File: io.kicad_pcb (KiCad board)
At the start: 2 copper layers, 107 x 58 mm, 98 parts, among them P1 CONN_01X04, P2 CONN_01X04, P3 CONN_01X04, P4 CONN_02X06, P5 CONN_02X09, Q1 VND7NV04, Q2 VND7NV04, Q3 VND7NV04, Q4 VND7NV04, Q5 VND7NV04, Q6 VND7NV04, U1 TC4427, U2 TC4427, U3 TC4427, U4 MCP2562-H/P, U5 LM2940

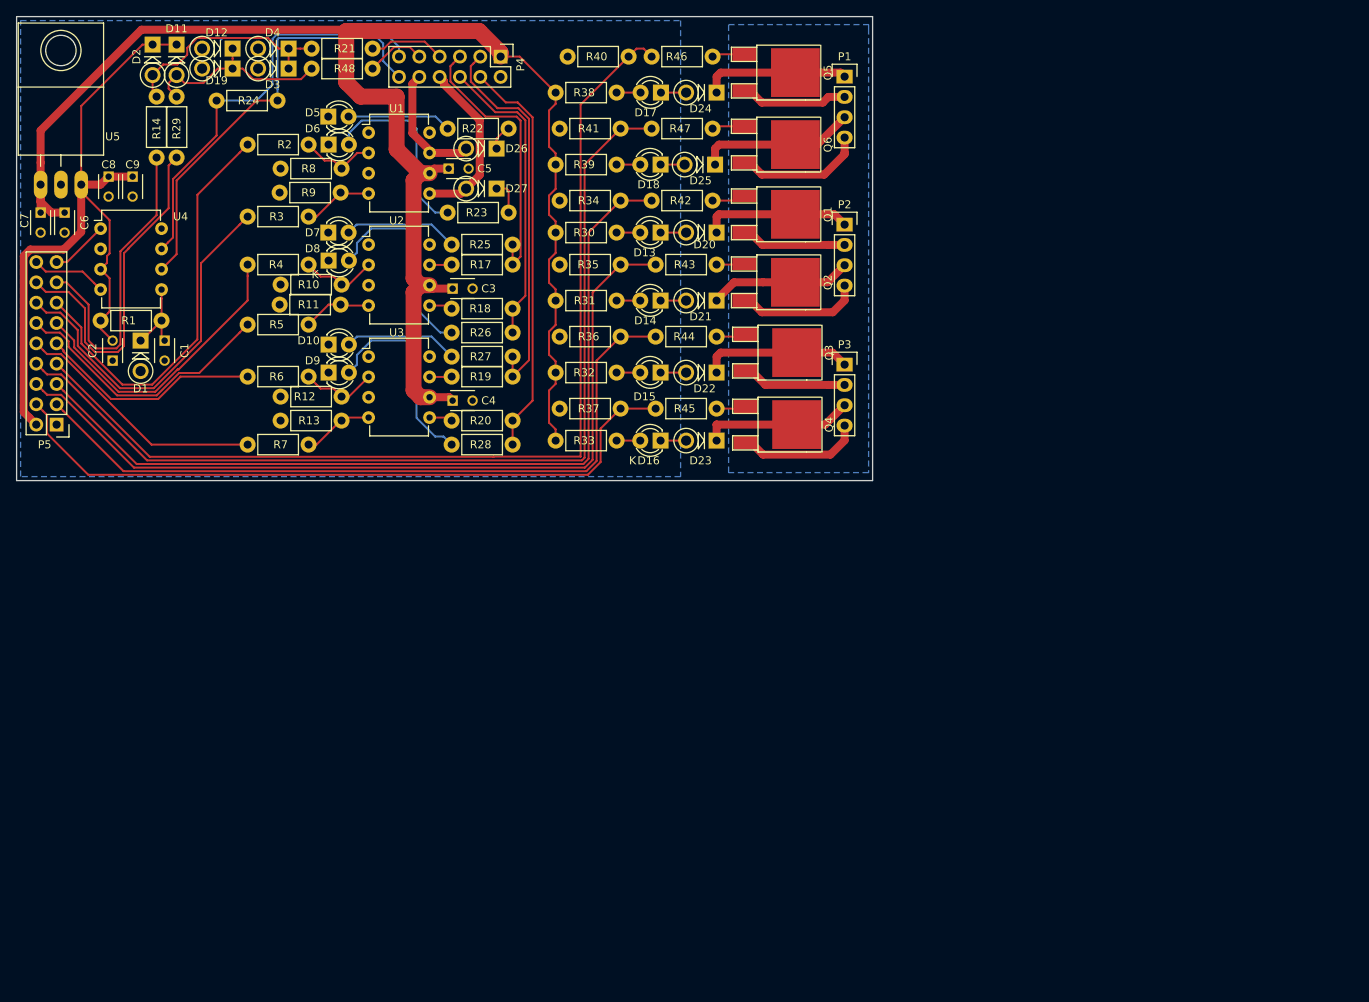
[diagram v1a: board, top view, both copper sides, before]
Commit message: Various updates to io board: - Add trigger inputs - Switch to 3v logic fets - switch to SMT components
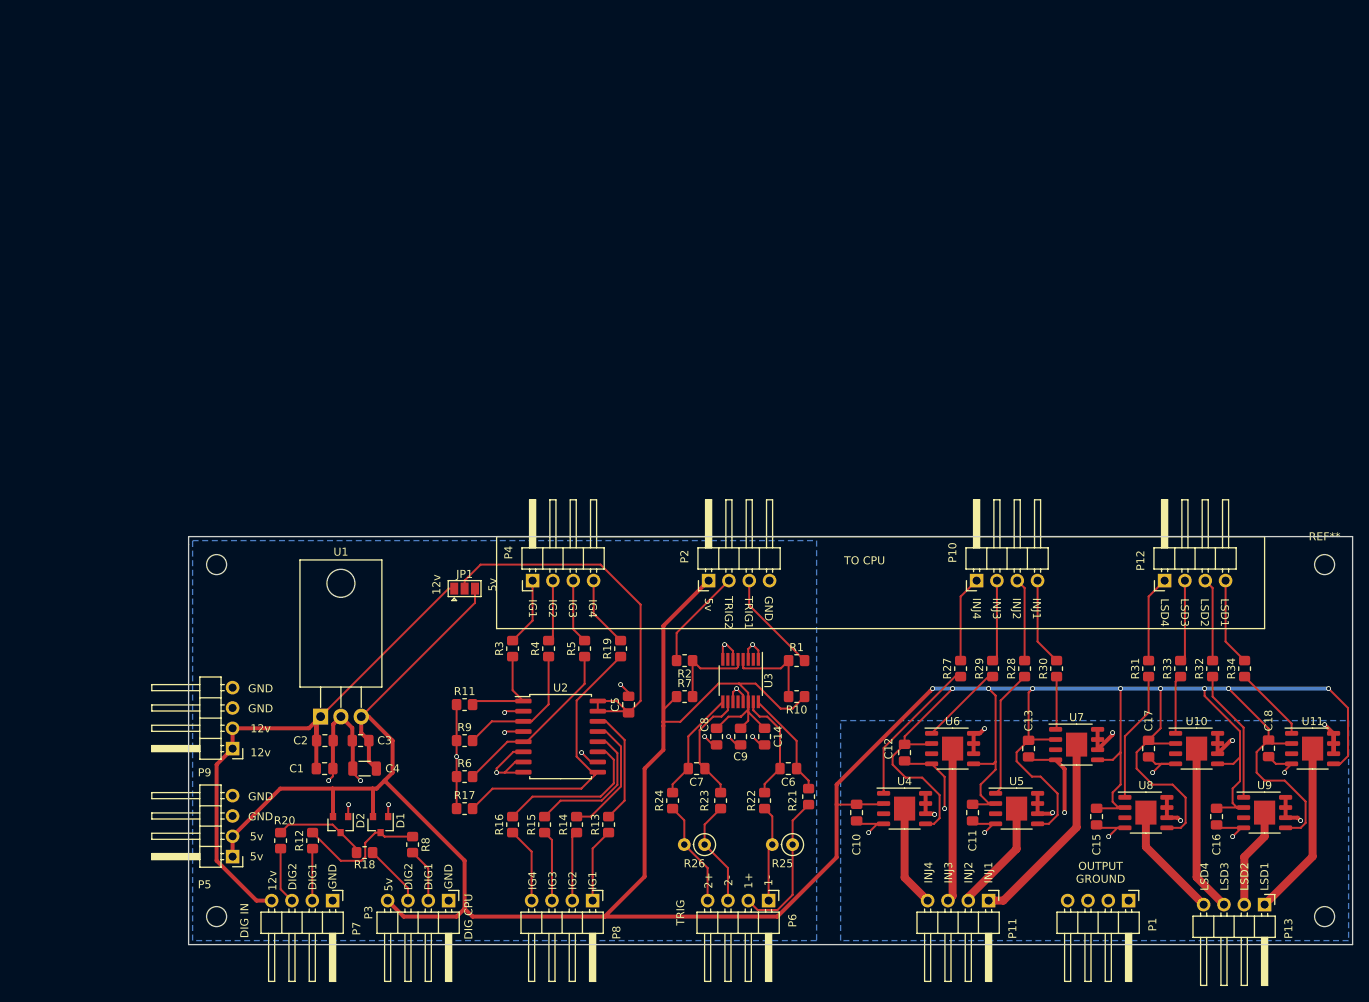
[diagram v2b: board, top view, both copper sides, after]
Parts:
- removed D10, D13, D14, D15, D16, D17, D18, D5, D6, D7, D8, D9: LED, LEDs:LED-3MM
- removed D11, D12, D20, D21, D22, D23, D24, D25, D26, D27, D3: D, Diodes_ThroughHole:Diode_DO-41_SOD81_Vertical_KathodeUp
- removed D19, D4: D_Zener, Diodes_ThroughHole:Diode_DO-41_SOD81_Vertical_KathodeUp
- removed Q1, Q2, Q3, Q4, Q5, Q6: VND7NV04, TO_SOT_Packages_SMD:TO-252-2Lead
- removed R35, R36, R37, R40, R41: 100k, Resistors_ThroughHole:Resistor_Horizontal_RM7mm
- removed R38, R39: 2.43k, Resistors_ThroughHole:Resistor_Horizontal_RM7mm
- removed R42, R43, R44, R45, R46, R47: 330, Resistors_ThroughHole:Resistor_Horizontal_RM7mm
- removed R48: 1k, Resistors_ThroughHole:Resistor_Horizontal_RM7mm
- added C10: .1uF, Capacitor_SMD:C_0805_2012Metric_Pad1.18x1.45mm_HandSolder, F.Cu at (118.5, 140.0)
- added C11: .1uF, Capacitor_SMD:C_0805_2012Metric_Pad1.18x1.45mm_HandSolder, F.Cu at (133.0, 140.0)
- added C12: .1uF, Capacitor_SMD:C_0805_2012Metric_Pad1.18x1.45mm_HandSolder, F.Cu at (124.5, 132.5)
- added C13: .1uF, Capacitor_SMD:C_0805_2012Metric_Pad1.18x1.45mm_HandSolder, F.Cu at (140.0, 132.0)
- added C14: 1u, Capacitor_SMD:C_0805_2012Metric_Pad1.18x1.45mm_HandSolder, F.Cu at (107.0, 130.5)
- added C15: .1uF, Capacitor_SMD:C_0805_2012Metric_Pad1.18x1.45mm_HandSolder, F.Cu at (148.5, 140.5)
- added C16: .1uF, Capacitor_SMD:C_0805_2012Metric_Pad1.18x1.45mm_HandSolder, F.Cu at (163.5, 140.5)
- added C17: .1uF, Capacitor_SMD:C_0805_2012Metric_Pad1.18x1.45mm_HandSolder, F.Cu at (155.0, 132.0)
- added C18: .1uF, Capacitor_SMD:C_0805_2012Metric_Pad1.18x1.45mm_HandSolder, F.Cu at (170.0, 132.0)
- added JP1: IG_PWR, Jumper:SolderJumper-3_P1.3mm_Open_Pad1.0x1.5mm, F.Cu at (69.5, 112.0)
- added P10: INJ-CPU, Connector_PinHeader_2.54mm:PinHeader_1x04_P2.54mm_Horizontal, F.Cu at (133.5, 111.0)
- added P11: INJECTORS, Connector_PinHeader_2.54mm:PinHeader_1x04_P2.54mm_Horizontal, F.Cu at (135.0, 151.0)
- added P12: LSD-CPU, Connector_PinHeader_2.54mm:PinHeader_1x04_P2.54mm_Horizontal, F.Cu at (157.0, 111.0)
- added P13: LSDS, Connector_PinHeader_2.54mm:PinHeader_1x04_P2.54mm_Horizontal, F.Cu at (169.5, 151.5)
- added P6: TRIG-IN, Connector_PinHeader_2.54mm:PinHeader_1x04_P2.54mm_Horizontal, F.Cu at (107.5, 151.0)
- added P7: DIG-IN, Connector_PinHeader_2.54mm:PinHeader_1x04_P2.54mm_Horizontal, F.Cu at (53.0, 151.0)
- added P8: IGNITION, Connector_PinHeader_2.54mm:PinHeader_1x04_P2.54mm_Horizontal, F.Cu at (85.5, 151.0)
- added P9: PWR_IN, Connector_PinHeader_2.54mm:PinHeader_1x04_P2.54mm_Horizontal, F.Cu at (40.5, 132.0)
- added R15: 150, Resistor_SMD:R_0805_2012Metric_Pad1.20x1.40mm_HandSolder, F.Cu at (79.5, 141.5)
- added R16: 150, Resistor_SMD:R_0805_2012Metric_Pad1.20x1.40mm_HandSolder, F.Cu at (75.5, 141.5)
- added REF**: MountingHole_2.5mm, MountingHole:MountingHole_2.5mm, F.Cu at (177.0, 109.0)
- added REF**: MountingHole_2.5mm, MountingHole:MountingHole_2.5mm, F.Cu at (177.0, 153.0)
- added REF**: MountingHole_2.5mm, MountingHole:MountingHole_2.5mm, F.Cu at (38.5, 153.0)
- added REF**: MountingHole_2.5mm, MountingHole:MountingHole_2.5mm, F.Cu at (38.5, 109.0)
- added U10: BTF3080EJ, Package_SO:Infineon_PG-DSO-8-27_3.9x4.9mm_EP2.65x3mm, F.Cu at (161.0, 132.0)
- added U11: BTF3080EJ, Package_SO:Infineon_PG-DSO-8-27_3.9x4.9mm_EP2.65x3mm, F.Cu at (175.5, 132.0)
- added U6: BTF3080EJ, Package_SO:Infineon_PG-DSO-8-27_3.9x4.9mm_EP2.65x3mm, F.Cu at (130.5, 132.0)
- added U7: BTF3080EJ, Package_SO:Infineon_PG-DSO-8-27_3.9x4.9mm_EP2.65x3mm, F.Cu at (146.0, 131.5)
- added U8: BTF3080EJ, Package_SO:Infineon_PG-DSO-8-27_3.9x4.9mm_EP2.65x3mm, F.Cu at (154.7, 140.0)
- added U9: BTF3080EJ, Package_SO:Infineon_PG-DSO-8-27_3.9x4.9mm_EP2.65x3mm, F.Cu at (169.5, 140.0)
- C1: value 0.1 uF -> 10 uF; footprint Capacitors_ThroughHole:C_Disc_D3_P2.5 -> Capacitor_SMD:C_0805_2012Metric_Pad1.18x1.45mm_HandSolder
- C2, C5: footprint Capacitors_ThroughHole:C_Disc_D3_P2.5 -> Capacitor_SMD:C_0805_2012Metric_Pad1.18x1.45mm_HandSolder
- C3: value 1 uF -> 0.1 uF; footprint Capacitors_ThroughHole:C_Disc_D3_P2.5 -> Capacitor_SMD:C_0805_2012Metric_Pad1.18x1.45mm_HandSolder
- C4: value 1 uF -> 47 uF; footprint Capacitors_ThroughHole:C_Disc_D3_P2.5 -> Capacitor_SMD:C_1206_3216Metric
- C6: value 10 uF -> 1n; footprint Capacitors_ThroughHole:C_Disc_D3_P2.5 -> Capacitor_SMD:C_0805_2012Metric_Pad1.18x1.45mm_HandSolder
- C7: value 0.1 uF -> 1n; footprint Capacitors_ThroughHole:C_Disc_D3_P2.5 -> Capacitor_SMD:C_0805_2012Metric_Pad1.18x1.45mm_HandSolder
- C8: value 0.1 uF -> 10n; footprint Capacitors_ThroughHole:C_Disc_D3_P2.5 -> Capacitor_SMD:C_0805_2012Metric_Pad1.18x1.45mm_HandSolder
- C9: value 47 uF -> 0.1u; footprint Capacitors_ThroughHole:C_Disc_D3_P2.5 -> Capacitor_SMD:C_0805_2012Metric_Pad1.18x1.45mm_HandSolder
- D1: value 3.3 V Zener -> BAT54S; footprint Diodes_ThroughHole:Diode_DO-41_SOD81_Vertical_KathodeUp -> Package_TO_SOT_SMD:SOT-23
- D2: value D -> BAT54S; footprint Diodes_ThroughHole:Diode_DO-41_SOD81_Vertical_KathodeUp -> Package_TO_SOT_SMD:SOT-23
- P1: value CONN_01X04 -> OUT_GND; footprint Pin_Headers:Pin_Header_Straight_1x04 -> Connector_PinHeader_2.54mm:PinHeader_1x04_P2.54mm_Horizontal
- P2: value CONN_01X04 -> TRIG-cpu; footprint Pin_Headers:Pin_Header_Straight_1x04 -> Connector_PinHeader_2.54mm:PinHeader_1x04_P2.54mm_Horizontal
- P3: value CONN_01X04 -> DIG-CPU; footprint Pin_Headers:Pin_Header_Straight_1x04 -> Connector_PinHeader_2.54mm:PinHeader_1x04_P2.54mm_Horizontal
- P4: value CONN_02X06 -> IN-CPU; footprint Pin_Headers:Pin_Header_Straight_2x06 -> Connector_PinHeader_2.54mm:PinHeader_1x04_P2.54mm_Horizontal
- P5: value CONN_02X09 -> CPU_PWR; footprint Pin_Headers:Pin_Header_Straight_2x09 -> Connector_PinHeader_2.54mm:PinHeader_1x04_P2.54mm_Horizontal
- R1, R11, R2, R21, R29, R3, R4, R5, R9: footprint Resistors_ThroughHole:Resistor_Horizontal_RM7mm -> Resistor_SMD:R_0805_2012Metric_Pad1.20x1.40mm_HandSolder
- R10: value 100k -> 10k; footprint Resistors_ThroughHole:Resistor_Horizontal_RM7mm -> Resistor_SMD:R_0805_2012Metric_Pad1.20x1.40mm_HandSolder
- R12, R34, R8: value 100k -> 1k; footprint Resistors_ThroughHole:Resistor_Horizontal_RM7mm -> Resistor_SMD:R_0805_2012Metric_Pad1.20x1.40mm_HandSolder
- R13: value 100k -> 150; footprint Resistors_ThroughHole:Resistor_Horizontal_RM7mm -> Resistor_SMD:R_0805_2012Metric_Pad1.20x1.40mm_HandSolder
- R14: value 1k -> 150; footprint Resistors_ThroughHole:Resistor_Horizontal_RM7mm -> Resistor_SMD:R_0805_2012Metric_Pad1.20x1.40mm_HandSolder
- R17: value 150 -> 100k; footprint Resistors_ThroughHole:Resistor_Horizontal_RM7mm -> Resistor_SMD:R_0805_2012Metric_Pad1.20x1.40mm_HandSolder
- R18, R19, R20: value 150 -> 1k; footprint Resistors_ThroughHole:Resistor_Horizontal_RM7mm -> Resistor_SMD:R_0805_2012Metric_Pad1.20x1.40mm_HandSolder
- R22, R23, R27, R28, R30, R31, R32, R33: value 2.43k -> 1k; footprint Resistors_ThroughHole:Resistor_Horizontal_RM7mm -> Resistor_SMD:R_0805_2012Metric_Pad1.20x1.40mm_HandSolder
- R24: value 120 -> 1k; footprint Resistors_ThroughHole:Resistor_Horizontal_RM7mm -> Resistor_SMD:R_0805_2012Metric_Pad1.20x1.40mm_HandSolder
- R25, R26: value 2.43k -> 330; footprint Resistors_ThroughHole:Resistor_Horizontal_RM7mm -> Resistor_THT:R_Axial_DIN0207_L6.3mm_D2.5mm_P2.54mm_Vertical
- R6: value 1k -> 100k; footprint Resistors_ThroughHole:Resistor_Horizontal_RM7mm -> Resistor_SMD:R_0805_2012Metric_Pad1.20x1.40mm_HandSolder
- R7: value 1k -> 10k; footprint Resistors_ThroughHole:Resistor_Horizontal_RM7mm -> Resistor_SMD:R_0805_2012Metric_Pad1.20x1.40mm_HandSolder
- U1: value TC4427 -> LM2940; footprint Housings_DIP:DIP-8_W7.62mm -> Package_TO_SOT_THT:TO-220-3_Horizontal_TabDown
- U2: value TC4427 -> MIC4469; footprint Housings_DIP:DIP-8_W7.62mm -> Package_SO:SOIC-16W_7.5x10.3mm_P1.27mm
- U3: value TC4427 -> MAX9926UAEE+; footprint Housings_DIP:DIP-8_W7.62mm -> Package_SO:QSOP-16_3.9x4.9mm_P0.635mm
- U4: value MCP2562-H/P -> BTF3080EJ; footprint Housings_DIP:DIP-8_W7.62mm -> Package_SO:Infineon_PG-DSO-8-27_3.9x4.9mm_EP2.65x3mm
- U5: value LM2940 -> BTF3080EJ; footprint TO_SOT_Packages_THT:TO-220_Neutral123_Horizontal_LargePads -> Package_SO:Infineon_PG-DSO-8-27_3.9x4.9mm_EP2.65x3mm
- moved U5 142.7 mm to (138.5, 139.5)
- moved R29 124.6 mm to (135.5, 122.0), turned to 90 degrees
- moved U4 123.9 mm to (124.5, 139.5)
- moved C6 114.1 mm to (110.0, 134.5), turned to 180 degrees
- moved P1 108.9 mm to (152.5, 151.0), turned to 270 degrees
- moved R21 108.2 mm to (112.5, 138.0), turned to 90 degrees
- moved C7 107.5 mm to (98.5, 134.5), turned to 180 degrees
- moved R14 105.1 mm to (83.5, 141.5), turned to 90 degrees
- moved R24 104.4 mm to (95.5, 138.5), turned to 90 degrees
- moved C8 103.3 mm to (101.0, 130.5)
- moved C9 103.3 mm to (104.0, 130.5)
- moved D2 100.3 mm to (54.0, 141.5)
- moved R34 97.5 mm to (167.0, 122.0), turned to 90 degrees
- moved R1 96.8 mm to (111.0, 121.0)
- moved R22 92.9 mm to (107.0, 138.5), turned to 90 degrees
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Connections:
- C1 pad 1: Net-(C1-Pad1) -> 12v_power
- C2 pad 1: GND -> 12v_power
- C2 pad 2: 5v_cpu -> GND
- C3 pad 1: 12v_power -> 5v
- C4 pad 1: 12v_power -> 5v
- C5 pad 1: 12v_power -> Net-(C5-Pad1)
- C6 pad 1: 12v_power -> Net-(C6-Pad1)
- C6 pad 2: GND -> Net-(C6-Pad2)
- C7 pad 1: 12v_power -> Net-(C7-Pad1)
- C7 pad 2: GND -> Net-(C7-Pad2)
- C8 pad 1: 5v_cpu -> 5v
- C9 pad 1: 5v_cpu -> 5v
- D1 pad 1: Net-(C1-Pad1) -> GND
- D1 pad 2: GND -> 5v
- D2 pad 1: 5v_cpu -> GND
- D2 pad 2: Net-(D2-Pad2) -> 5v
- P1 pad 1: LSD1-out -> OUT_GND
- P1 pad 3: LSD2-out -> OUT_GND
- P2 pad 1: INJ1-out -> 5v
- P2 pad 2: OUT_GND -> TRIG2
- P2 pad 3: INJ2-out -> TRIG1
- P2 pad 4: OUT_GND -> GND
- P3 pad 1: INJ3-out -> GND
- P3 pad 2: OUT_GND -> DIG1-cpu
- P3 pad 3: INJ4-out -> DIG2-cpu
- P3 pad 4: OUT_GND -> 5v
- P4 pad 1: 12v_power -> IG1-cpu
- P4 pad 2: GND -> IG2-cpu
- P4 pad 3: IG3-out -> IG3-cpu
- P4 pad 4: IG4-out -> IG4-cpu
- P5 pad 1: GND -> 5v
- P5 pad 2: 5v_cpu -> 5v
- P5 pad 3: INJ3-cpu -> GND
- P5 pad 4: INJ4-cpu -> GND
- R1 pad 1: 5v_cpu -> Net-(R1-Pad1)
- R1 pad 2: Net-(C1-Pad1) -> TRIG1
- R10 pad 1: GND -> 5v
- R10 pad 2: Net-(R10-Pad2) -> Net-(R1-Pad1)
- R11 pad 1: Net-(R11-Pad1) -> GND
- R11 pad 2: GND -> Net-(R11-Pad2)
- R12 pad 1: GND -> DIG1-in
- R12 pad 2: Net-(R12-Pad2) -> Net-(D1-Pad3)
- R13 pad 1: Net-(R13-Pad1) -> IG1-out
- R13 pad 2: GND -> Net-(R13-Pad2)
- R14 pad 1: Net-(D2-Pad2) -> IG2-out
- R14 pad 2: DIG1-cpu -> Net-(R14-Pad2)
- R17 pad 1: IG1-out -> GND
- R18 pad 1: IG2-out -> Net-(D2-Pad3)
- R18 pad 2: Net-(R18-Pad2) -> DIG2-cpu
- R19 pad 1: IG3-out -> Net-(R17-Pad2)
- R19 pad 2: Net-(R19-Pad2) -> IG4-cpu
- R2 pad 2: HSD1-cpu -> TRIG2
- R20 pad 1: IG4-out -> DIG2-in
- R20 pad 2: Net-(R20-Pad2) -> Net-(D2-Pad3)
- R21 pad 1: DIG1-in -> TRIG1IN+
- R21 pad 2: Net-(D2-Pad2) -> Net-(C6-Pad1)
- R22 pad 1: Net-(D5-Pad2) -> TRIG1IN-
- R22 pad 2: Net-(D26-Pad1) -> Net-(C6-Pad2)
- R23 pad 1: Net-(D27-Pad1) -> TRIG2IN-
- R23 pad 2: Net-(D6-Pad2) -> Net-(C7-Pad1)
- R24 pad 1: CAN_H -> TRIG2IN+
- R24 pad 2: CAN_L -> Net-(C7-Pad2)
- R25 pad 1: IG1-out -> TRIG1IN+
- R25 pad 2: Net-(D7-Pad2) -> TRIG1IN-
- R26 pad 1: IG2-out -> TRIG2IN-
- R26 pad 2: Net-(D8-Pad2) -> TRIG2IN+
- R27 pad 1: IG3-out -> Net-(R27-Pad1)
- R27 pad 2: Net-(D9-Pad2) -> INJ4-cpu
- R28 pad 1: IG4-out -> Net-(R28-Pad1)
- R28 pad 2: Net-(D10-Pad2) -> INJ2-cpu
- R29 pad 2: DIG2-cpu -> INJ3-cpu
- R3 pad 1: Net-(R3-Pad1) -> Net-(R11-Pad2)
- R3 pad 2: HSD2-cpu -> IG1-cpu
- R30 pad 2: 12v_power -> INJ1-cpu
- R31 pad 2: 12v_power -> LSD4-cpu
- R32 pad 2: 12v_power -> LSD2-cpu
- R33 pad 2: 12v_power -> LSD3-cpu
- R34 pad 1: INJ1-cpu -> Net-(R34-Pad1)
- R34 pad 2: GND -> LSD1-cpu
- R4 pad 1: Net-(R10-Pad2) -> Net-(R4-Pad1)
- R4 pad 2: IG1-cpu -> IG2-cpu
- R5 pad 1: Net-(R11-Pad1) -> Net-(R5-Pad1)
- R5 pad 2: IG2-cpu -> IG3-cpu
- R6 pad 1: Net-(R12-Pad2) -> GND
- R6 pad 2: IG3-cpu -> Net-(R5-Pad1)
- R7 pad 1: Net-(R13-Pad1) -> 5v
- R7 pad 2: IG4-cpu -> Net-(R2-Pad1)
- R8 pad 1: GND -> Net-(D1-Pad3)
- R8 pad 2: Net-(R2-Pad1) -> DIG1-cpu
- R9 pad 1: Net-(R3-Pad1) -> GND
- R9 pad 2: GND -> Net-(R4-Pad1)
- U1 pad 1: (no net) -> 12v_power
- U1 pad 2: Net-(R2-Pad1) -> GND
- U1 pad 3: GND -> 5v
- U2 pad 1: (no net) -> Net-(R11-Pad2)
- U2 pad 2: Net-(R10-Pad2) -> GND
- U2 pad 3: GND -> Net-(R4-Pad1)
- U2 pad 4: Net-(R11-Pad1) -> GND
- U2 pad 5: Net-(R18-Pad2) -> Net-(R5-Pad1)
- U2 pad 6: 12v_power -> GND
- U2 pad 7: Net-(R17-Pad2) -> GND
- U2 pad 8: (no net) -> GND
- U3 pad 1: (no net) -> GND
- U3 pad 2: Net-(R12-Pad2) -> (no net)
- U3 pad 4: Net-(R13-Pad1) -> Net-(R1-Pad1)
- U3 pad 5: Net-(R20-Pad2) -> Net-(R2-Pad1)
- U3 pad 6: 12v_power -> GND
- U3 pad 7: Net-(R19-Pad2) -> (no net)
- U3 pad 8: (no net) -> GND
- U4 pad 1: CAN_TX -> Net-(R27-Pad1)
- U4 pad 2: GND -> 5v
- U4 pad 3: 5v_cpu -> (no net)
- U4 pad 4: CAN_RX -> OUT_GND
- U4 pad 5: Net-(C1-Pad1) -> 5v
- U4 pad 6: CAN_L -> OUT_GND
- U4 pad 7: CAN_H -> OUT_GND
- U4 pad 8: GND -> OUT_GND
- U5 pad 1: 12v_power -> Net-(R28-Pad1)
- U5 pad 2: GND -> 5v
- U5 pad 3: 5v_cpu -> (no net)
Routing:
- net 5v: track 0.00 -> 516.8 mm, vias 0 -> 9
- net 12v_power: track 202.1 -> 71.2 mm
- net LSD1-cpu: track 126.5 -> 11.0 mm
- net LSD2-cpu: track 120.6 -> 10.4 mm
- net INJ1-cpu: track 108.7 -> 11.0 mm
- net INJ2-cpu: track 104.5 -> 10.4 mm
- net 5v_cpu: track 90.8 -> 0.00 mm
- net INJ3-cpu: track 92.7 -> 10.2 mm
- net INJ4-cpu: track 88.3 -> 10.8 mm
- net GND: track 0.00 -> 72.1 mm, vias 0 -> 16
- net CAN_L: track 54.9 -> 0.00 mm
- net CAN_H: track 52.8 -> 0.00 mm
- net HSD1-cpu: track 52.3 -> 0.00 mm
- net Net-(C5-Pad1): track 0.00 -> 49.7 mm
- net HSD2-cpu: track 46.6 -> 0.00 mm
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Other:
- board size 107 x 58 mm -> 145.5 x 51 mm
- board text added: "1+"
- board text added: "1-"
- board text added: "12v"
- board text added: "2+"
- board text added: "2-"
- board text added: "5v"
- board text added: "DIG CPU"
- board text added: "DIG IN"
- board text added: "DIG1"
- board text added: "DIG2"
- board text added: "GND"
- board text added: "IG1"
- board text added: "IG2"
- board text added: "IG3"
- board text added: "IG4"
- board text added: "INJ1"
- board text added: "INJ2"
- board text added: "INJ3"
- board text added: "INJ4"
- board text added: "LSD1"
- board text added: "LSD2"
- board text added: "LSD3"
- board text added: "LSD4"
- board text added: "OUTPUT GROUND"
- board text added: "TO CPU"
- board text added: "TRIG"
- board text added: "TRIG1"
- board text added: "TRIG2"
